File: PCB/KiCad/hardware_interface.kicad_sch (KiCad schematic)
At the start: 5 parts

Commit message: add final traces
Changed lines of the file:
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@@
 	)
 	(no_connect
+		(at 39.37 111.76)
+	)
+	(no_connect
 		(at 157.48 132.08)
 	)
@@
 	)
 	(no_connect
-		(at 39.37 139.7)
+		(at 157.48 129.54)
 	)
 	(no_connect
@@
 	)
 	(no_connect
-		(at 39.37 86.36)
-	)
-	(no_connect
 		(at 39.37 137.16)
 	)
@@
 		)
 	)
-	(global_label "PWR_EXT_EN"
-		(shape output)
-		(at 39.37 111.76 180)
-		(fields_autoplaced yes)
-		(effects
-			(font
-				(size 1.016 1.016)
-			)
-			(justify right)
-		)
-		(property "Intersheetrefs" "${INTERSHEET_REFS}"
-			(at 27.5963 111.76 0)
-			(effects
-				(font
-					(size 1.27 1.27)
-				)
-				(justify right)
-				(hide yes)
-			)
-		)
-	)
 	(global_label "SPI1_CS2'"
 		(shape output)
@@
 		)
 	)
-	(global_label "USER_BUTTON"
-		(shape input)
-		(at 157.48 129.54 0)
-		(fields_autoplaced yes)
-		(effects
-			(font
-				(size 1.016 1.016)
-			)
-			(justify left)
-		)
-		(property "Intersheetrefs" "${INTERSHEET_REFS}"
-			(at 170.3666 129.54 0)
-			(effects
-				(font
-					(size 1.27 1.27)
-				)
-				(justify left)
-				(hide yes)
-			)
-		)
-	)
 	(global_label "SPI1_CS1'"
 		(shape output)
@@
 		)
 	)
+	(global_label "PWR_EXT_EN"
+		(shape output)
+		(at 39.37 139.7 180)
+		(fields_autoplaced yes)
+		(effects
+			(font
+				(size 1.016 1.016)
+			)
+			(justify right)
+		)
+		(property "Intersheetrefs" "${INTERSHEET_REFS}"
+			(at 27.5963 139.7 0)
+			(effects
+				(font
+					(size 1.27 1.27)
+				)
+				(justify right)
+				(hide yes)
+			)
+		)
+	)
 	(global_label "TIM1_CH1'"
 		(shape bidirectional)
@@
 				(hide yes)
 			)
+		)
+	)
+	(global_label "USER_BUTTON"
+		(shape input)
+		(at 39.37 86.36 180)
+		(fields_autoplaced yes)
+		(effects
+			(font
+				(size 1.016 1.016)
+			)
+			(justify right)
+		)
+		(property "Intersheetrefs" "${INTERSHEET_REFS}"
+			(at 26.4834 86.36 0)
+			(effects
+				(font
+					(size 1.27 1.27)
+				)
+				(justify right)
+				(hide yes)
+			)

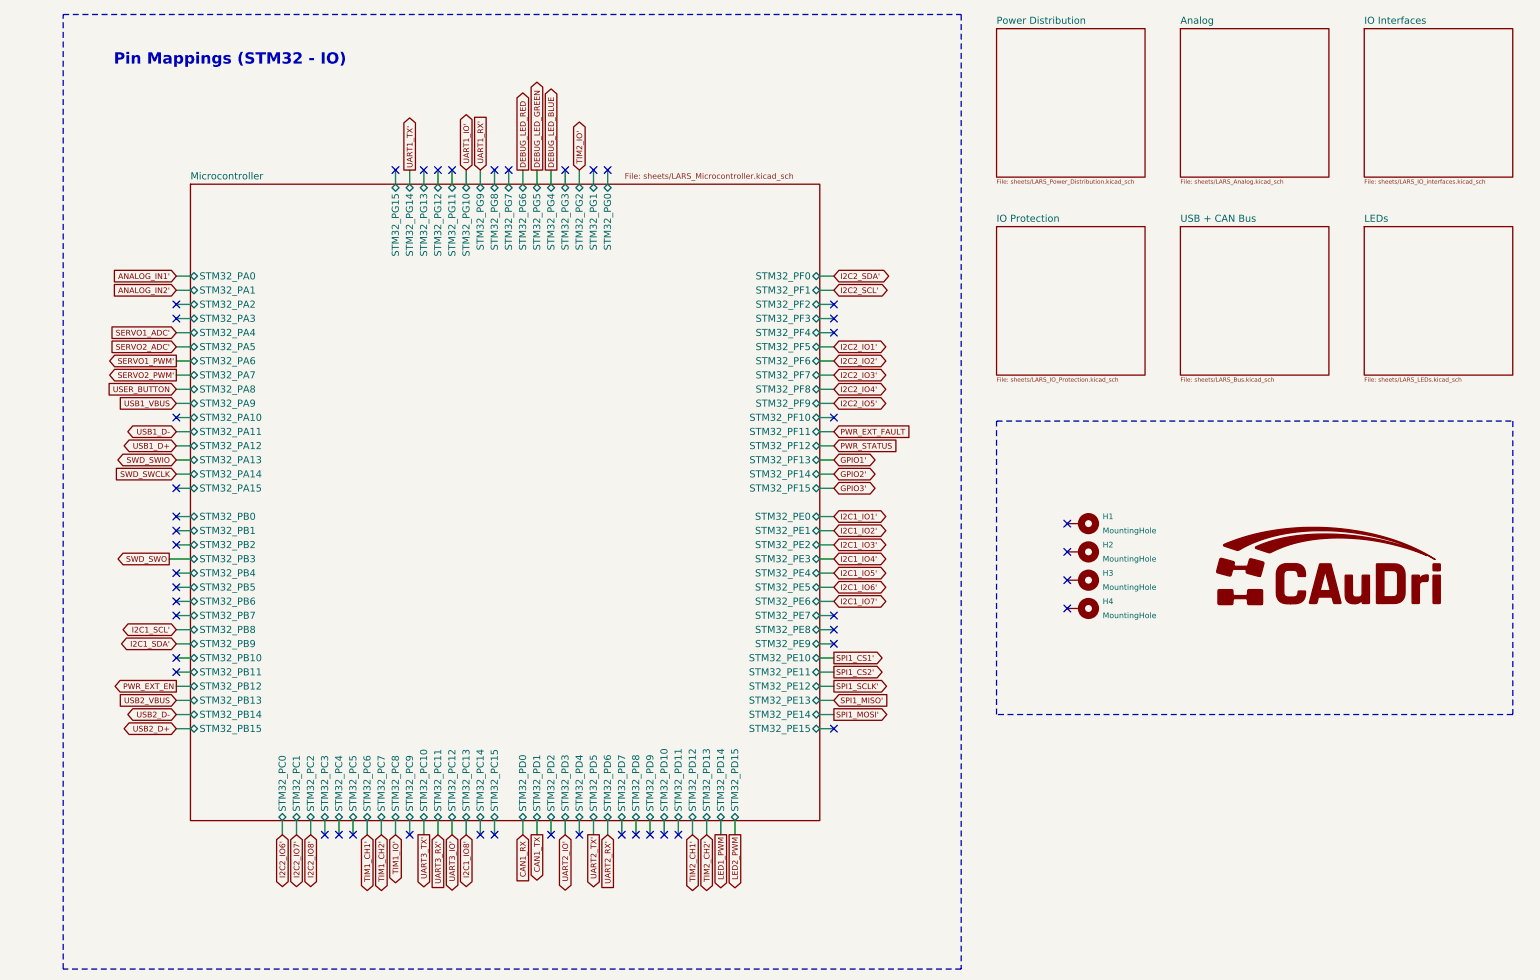
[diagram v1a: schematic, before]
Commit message: change default KiCad schematic font
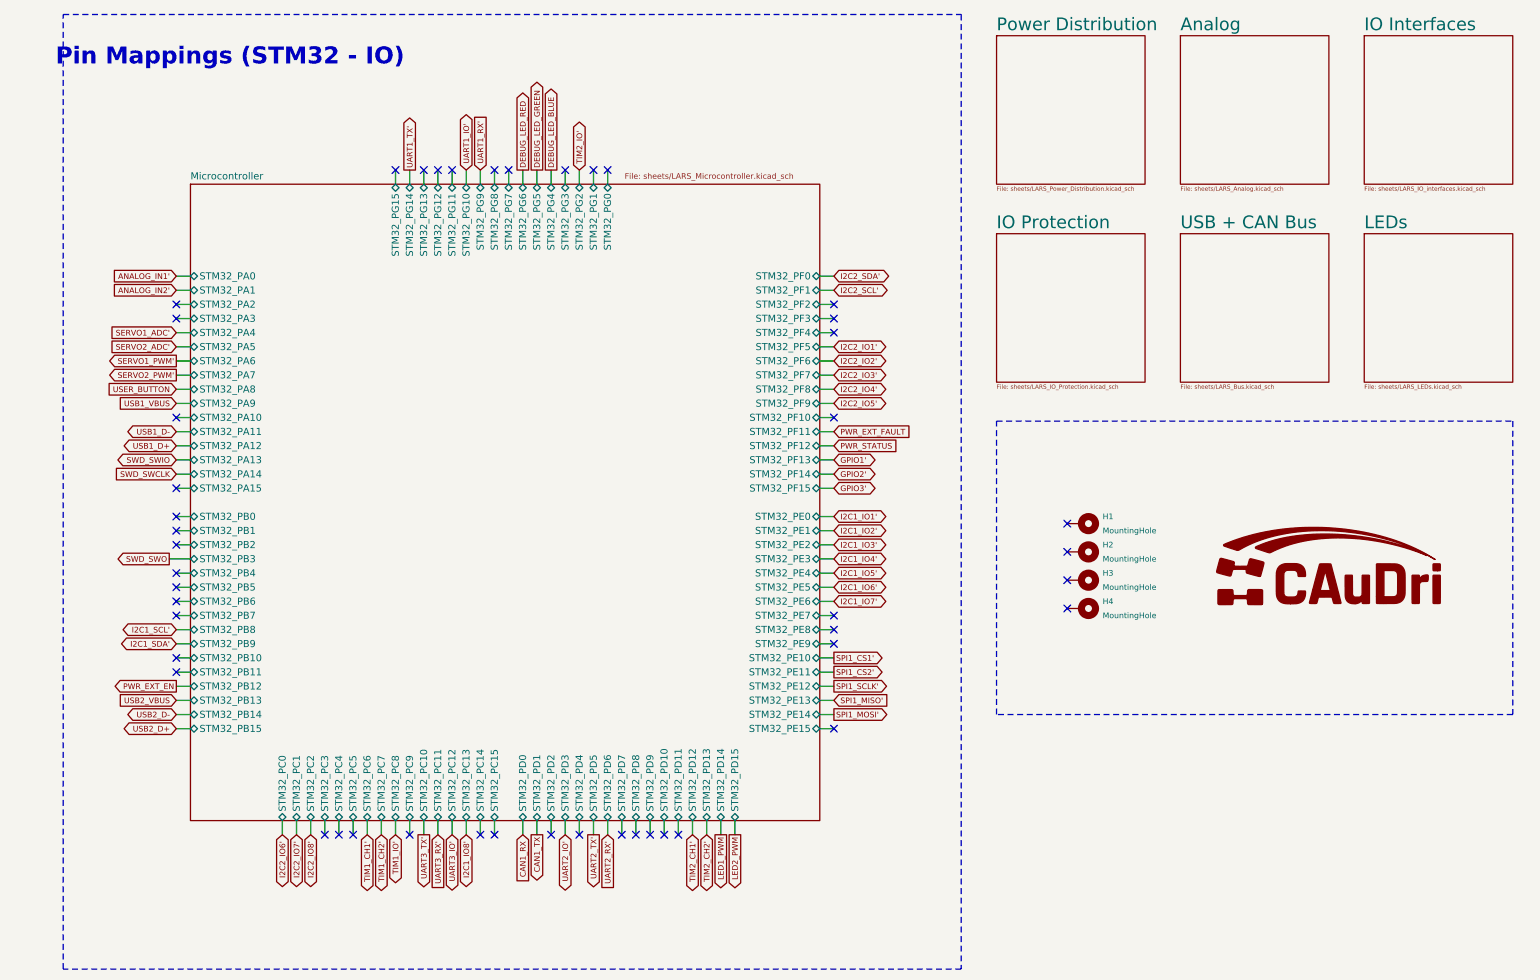
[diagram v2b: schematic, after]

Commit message: update text layout and fix remaining DRC errors
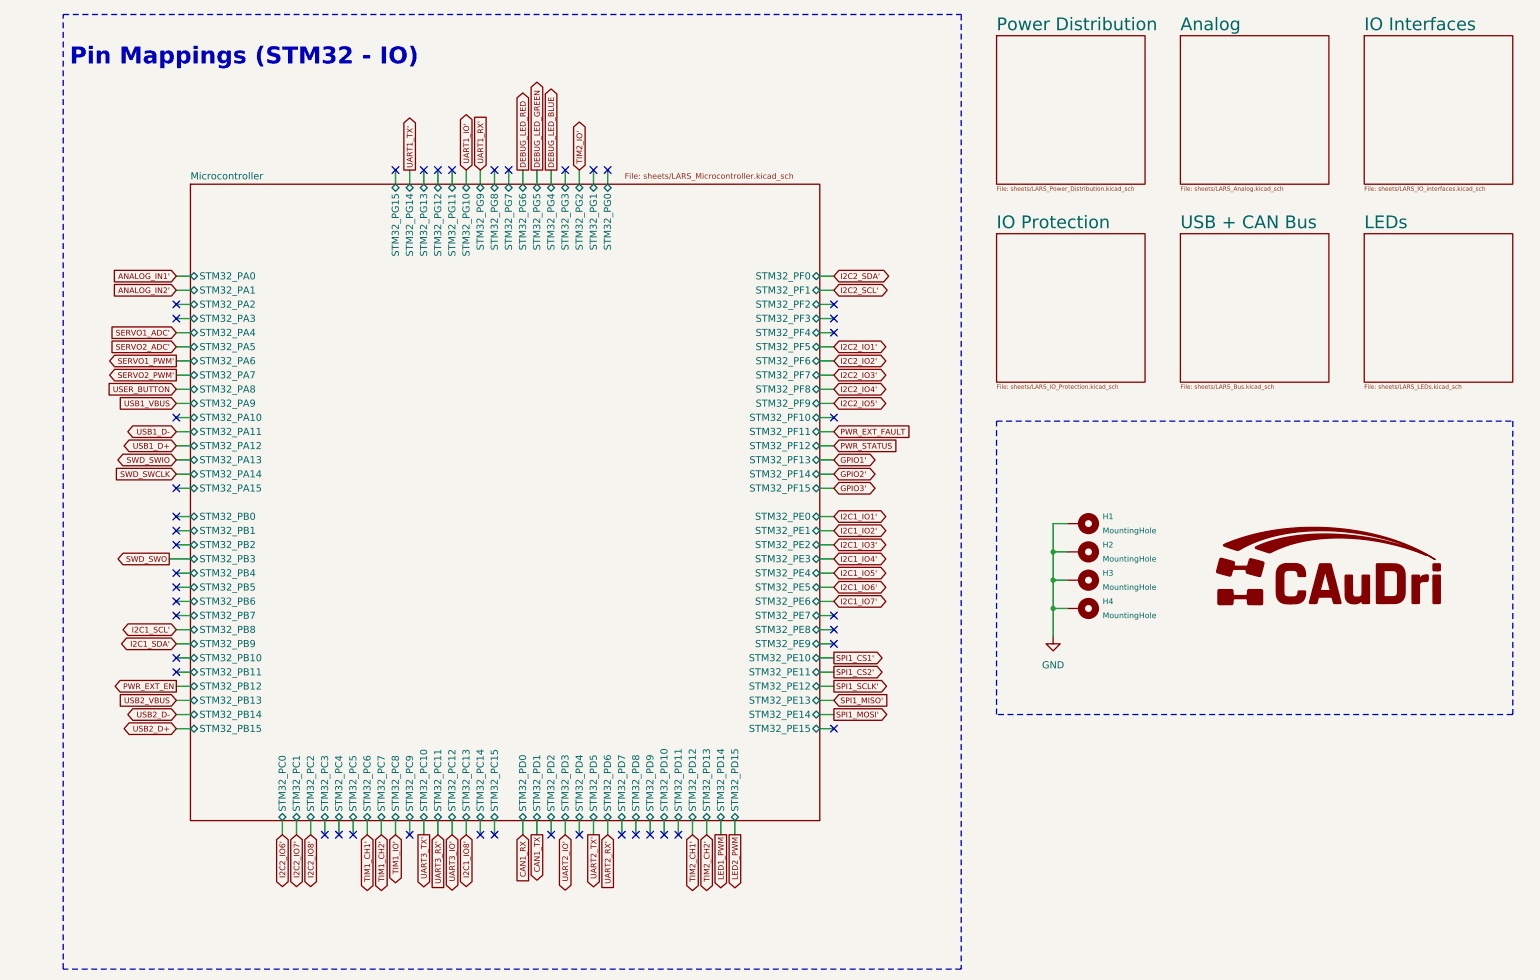
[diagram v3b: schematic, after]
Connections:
- net GND: now reaches H3.1
- net GND: now also H1.1, H2.1, H4.1
- no-connect marks 47 -> 43
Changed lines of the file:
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@@
 	(text "Pin Mappings (STM32 - IO)"
 		(exclude_from_sim no)
-		(at 49.022 26.67 0)
+		(at 51.562 26.67 0)
 		(effects
 			(font
@@
 		)
 	)
+	(junction
+		(at 196.85 120.65)
+		(diameter 0)
+		(color 0 0 0 0)
+	)
+	(junction
+		(at 196.85 125.73)
+		(diameter 0)
+		(color 0 0 0 0)
+	)
+	(junction
+		(at 196.85 115.57)
+		(diameter 0)
+		(color 0 0 0 0)
+	)
 	(no_connect
 		(at 93.98 166.37)
@@
 	)
 	(no_connect
-		(at 199.39 125.73)
-	)
-	(no_connect
 		(at 81.28 166.37)
 	)
@@
 	)
 	(no_connect
-		(at 199.39 120.65)
-	)
-	(no_connect
 		(at 109.22 46.99)
 	)
@@
 	)
 	(no_connect
-		(at 199.39 115.57)
-	)
-	(no_connect
 		(at 39.37 137.16)
 	)
@@
 	)
 	(no_connect
-		(at 199.39 110.49)
-	)
-	(no_connect
 		(at 39.37 109.22)
 	)
@@
 	(wire
 		(pts
+			(xy 196.85 120.65) (xy 196.85 115.57)
+		)
+		(stroke
+			(width 0)
+			(type default)
+		)
+	)
+	(wire
+		(pts
 			(xy 39.37 81.28) (xy 41.91 81.28)
 		)
@@
 	(wire
 		(pts
+			(xy 196.85 110.49) (xy 199.39 110.49)
+		)
+		(stroke
+			(width 0)
+			(type default)
+		)
+	)
+	(wire
+		(pts
 			(xy 157.48 66.04) (xy 154.94 66.04)
 		)
@@
 	(wire
 		(pts
+			(xy 196.85 130.81) (xy 196.85 125.73)
+		)
+		(stroke
+			(width 0)
+			(type default)
+		)
+	)
+	(wire
+		(pts
 			(xy 157.48 104.14) (xy 154.94 104.14)
 		)
@@
 	(wire
 		(pts
+			(xy 196.85 125.73) (xy 196.85 120.65)
+		)
+		(stroke
+			(width 0)
+			(type default)
+		)
+	)
+	(wire
+		(pts
 			(xy 39.37 93.98) (xy 41.91 93.98)
 		)
@@
 	(wire
 		(pts
+			(xy 199.39 120.65) (xy 196.85 120.65)
+		)
+		(stroke
+			(width 0)
+			(type default)
+		)
+	)
+	(wire
+		(pts
 			(xy 154.94 86.36) (xy 157.48 86.36)
 		)
@@
 	(wire
 		(pts
+			(xy 199.39 125.73) (xy 196.85 125.73)
+		)
+		(stroke
+			(width 0)
+			(type default)
+		)
+	)
+	(wire
+		(pts
 			(xy 157.48 124.46) (xy 154.94 124.46)
 		)
@@
 	(wire
 		(pts
+			(xy 199.39 115.57) (xy 196.85 115.57)
+		)
+		(stroke
+			(width 0)
+			(type default)
+		)
+	)
+	(wire
+		(pts
 			(xy 39.37 76.2) (xy 41.91 76.2)
 		)
@@
 	(wire
 		(pts
+			(xy 196.85 115.57) (xy 196.85 110.49)
+		)
+		(stroke
+			(width 0)
+			(type default)
+		)
+	)
+	(wire
+		(pts
 			(xy 157.48 111.76) (xy 154.94 111.76)
 		)
@@
 	)
 	(symbol
+		(lib_id "power:GND")
+		(at 196.85 130.81 0)
+		(unit 1)
+		(exclude_from_sim no)
+		(in_bom yes)
+		(on_board yes)
+		(dnp no)
+		(fields_autoplaced yes)
+		(property "Reference" "#PWR0208"
+			(at 196.85 137.16 0)
+			(effects
+				(font
+					(size 1.27 1.27)
+				)
+				(hide yes)
+			)
+		)
+		(property "Value" "GND"
+			(at 196.85 135.89 0)
+			(effects
+				(font
+					(size 1.27 1.27)
+				)
+			)
+		)
+		(property "Footprint" ""
+			(at 196.85 130.81 0)
+			(effects
+				(font
+					(size 1.27 1.27)
+				)
+				(hide yes)
+			)
+		)
+		(property "Datasheet" ""
+			(at 196.85 130.81 0)
+			(effects
+				(font
+					(size 1.27 1.27)
+				)
+				(hide yes)
+			)
+		)
+		(property "Description" "Power symbol creates a global label with name \"GND\" , ground"
+			(at 196.85 130.81 0)
+			(effects
+				(font
+					(size 1.27 1.27)
+				)
+				(hide yes)
+			)
+		)
+		(pin "1"
+		)
+		(instances
+			(project "hardware_interface"
+				(path "/ffedf44c-a51a-4124-b6d3-e3f1f256e9ac"
+					(reference "#PWR0208")
+					(unit 1)
+				)
+			)
+		)
+	)
+	(symbol
 		(lib_id "LARS_Hardware_Interface:CAuDri-Logo")
 		(at 246.38 118.11 0)
@@
 				(font
 					(size 2.286 2.286)
+					(color 0 0 194 1)
 				)
 				(justify left bottom)
@@
 				(font
 					(size 2.286 2.286)
+					(color 0 0 194 1)
 				)
 				(justify left bottom)
@@
 				(font
 					(size 2.286 2.286)
+					(color 0 0 194 1)
 				)
 				(justify left bottom)
@@
 				(font
 					(size 2.286 2.286)
+					(color 0 0 194 1)
 				)
 				(justify left bottom)
@@
 				(font
 					(size 2.286 2.286)
+					(color 0 0 194 1)
 				)
 				(justify left bottom)
@@
 				(font
 					(size 2.286 2.286)
+					(color 0 0 194 1)
 				)
 				(justify left bottom)
